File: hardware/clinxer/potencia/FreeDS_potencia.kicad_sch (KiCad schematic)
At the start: 17 parts, among them J1 Screw_Terminal_01x04, J2 Conn_01x04, Q3 BTA26-600BW, U1 MOC3041M, U5 Modulo de Control PWM de pote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

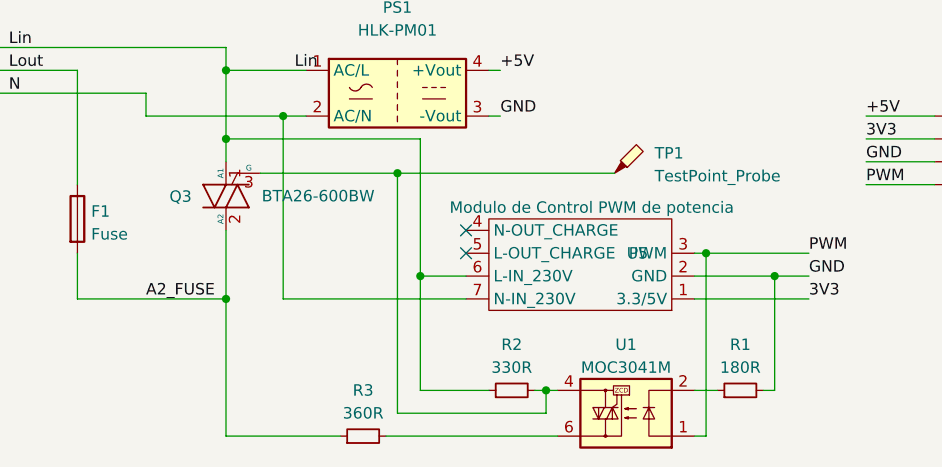
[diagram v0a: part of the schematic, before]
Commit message: Correcciones en arquitectura clinxer
Signed-off-by: Iván Sánchez Ortega <ivan@sanchezortega.es>
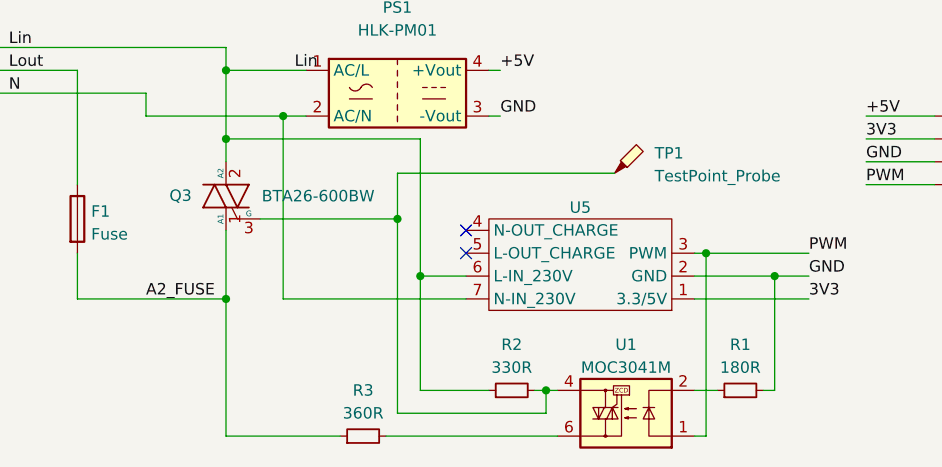
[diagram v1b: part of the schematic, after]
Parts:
- removed U5: Modulo de Control PWM de potencia, Module:YYAC-35 PWM TRIAC, symbol module:YYAC-35_PWM_TRIAC
- added U5: ~, Module:YYAC-3S PWM TRIAC, symbol module:YYAC-3S_PWM_TRIAC
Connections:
- net 3V3: now also U5.1 (3.3/5V)
- net A2_FUSE: now also Q3.1 (A1); no longer Q3.2 (A2)
- net GND: now also U5.2 (GND)
- net Lin: now also Q3.2 (A2), U5.6 (L-IN_230V); no longer Q3.1 (A1)
- net N: now also U5.7 (N-IN_230V)
- net PWM: now also U5.3 (PWM)
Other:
- moved on the sheet: Q3
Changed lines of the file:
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@@
 (kicad_sch (version 20230121) (generator eeschema)
   (paper "A4")
+  (junction (at 109.22 88.9) (diameter 0) (color 0 0 0 0)
+  )
   (junction (at 109.22 81.28) (diameter 0) (color 0 0 0 0)
   )
-  (junction (at 128.27 92.71) (diameter 0) (color 0 0 0 0)
+  (junction (at 128.27 97.79) (diameter 0) (color 0 0 0 0)
   )
   (junction (at 130.81 104.14) (diameter 0) (color 0 0 0 0)
   )
+  (junction (at 109.22 106.68) (diameter 0) (color 0 0 0 0)
+  )
   (junction (at 170.18 104.14) (diameter 0) (color 0 0 0 0)
   )
-  (junction (at 109.22 88.9) (diameter 0) (color 0 0 0 0)
-  )
   (junction (at 162.56 101.6) (diameter 0) (color 0 0 0 0)
-  )
-  (junction (at 109.22 106.68) (diameter 0) (color 0 0 0 0)
   )
   (junction (at 144.78 116.84) (diameter 0) (color 0 0 0 0)
@@
     (stroke (width 0) (type default))
   )
-  (wire (pts (xy 113.03 92.71) (xy 128.27 92.71))
-    (stroke (width 0) (type default))
-  )
   (wire (pts (xy 100.33 86.36) (xy 115.57 86.36))
     (stroke (width 0) (type default))
@@
     (stroke (width 0) (type default))
   )
-  (wire (pts (xy 128.27 92.71) (xy 128.27 119.38))
+  (wire (pts (xy 128.27 92.71) (xy 128.27 97.79))
     (stroke (width 0) (type default))
   )
@@
     (stroke (width 0) (type default))
   )
+  (wire (pts (xy 109.22 99.06) (xy 109.22 106.68))
+    (stroke (width 0) (type default))
+  )
   (wire (pts (xy 161.29 106.68) (xy 173.99 106.68))
     (stroke (width 0) (type default))
@@
     (stroke (width 0) (type default))
   )
+  (wire (pts (xy 113.03 97.79) (xy 128.27 97.79))
+    (stroke (width 0) (type default))
+  )
   (wire (pts (xy 170.18 104.14) (xy 173.99 104.14))
     (stroke (width 0) (type default))
@@
     (stroke (width 0) (type default))
   )
-  (wire (pts (xy 109.22 106.68) (xy 109.22 99.06))
-    (stroke (width 0) (type default))
-  )
   (wire (pts (xy 78.74 78.74) (xy 109.22 78.74))
     (stroke (width 0) (type default))
@@
   )
   (wire (pts (xy 81.28 86.36) (xy 81.28 91.44))
+    (stroke (width 0) (type default))
+  )
+  (wire (pts (xy 128.27 97.79) (xy 128.27 119.38))
     (stroke (width 0) (type default))
   )
@@
     )
   )
-  (symbol (lib_id "Triac_Thyristor:BTA16-600BW") (at 109.22 95.25 180) (unit 1)
+  (symbol (lib_id "Triac_Thyristor:BTA16-600BW") (at 109.22 95.25 0) (mirror y) (unit 1)
     (in_bom yes) (on_board yes) (dnp no)
-    (property "Reference" "Q3" (at 105.41 95.3008 0)
+    (property "Reference" "Q3" (at 105.41 95.1992 0)
       (effects (font (size 1.27 1.27)) (justify left))
     )
@@
       (effects (font (size 1.27 1.27)) (justify left))
     )
-    (property "Footprint" "Package_TO_SOT_THT:TOP3_Vertical" (at 104.14 93.345 0)
+    (property "Footprint" "Package_TO_SOT_THT:TOP3_Vertical" (at 104.14 97.155 0)
       (effects (font (size 1.27 1.27) italic) (justify left) hide)
     )
@@
     )
   )
-  (symbol (lib_id "module:YYAC-35_PWM_TRIAC") (at 153.67 105.41 180) (unit 1)
-    (in_bom yes) (on_board yes) (dnp no)
-    (property "Reference" "U5" (at 154.94 101.6 0)
-      (effects (font (size 1.27 1.27)))
-    )
-    (property "Value" "Modulo de Control PWM de potencia" (at 149.86 96.52 0)
-      (effects (font (size 1.27 1.27)))
-    )
-    (property "Footprint" "Module:YYAC-35 PWM TRIAC" (at 153.67 105.41 0)
+  (symbol (lib_id "Mechanical:MountingHole") (at 21.59 46.99 0) (unit 1)
+    (in_bom yes) (on_board yes) (dnp no) (fields_autoplaced)
+    (property "Reference" "H4" (at 24.13 46.355 0)
+      (effects (font (size 1.27 1.27)) (justify left))
+    )
+    (property "Value" "MountingHole" (at 24.13 48.895 0)
+      (effects (font (size 1.27 1.27)) (justify left))
+    )
+    (property "Footprint" "MountingHole:MountingHole_3.2mm_M3" (at 21.59 46.99 0)
+      (effects (font (size 1.27 1.27)) hide)
+    )
+    (property "Datasheet" "~" (at 21.59 46.99 0)
+      (effects (font (size 1.27 1.27)) hide)
+    )
+    (instances
+      (project "FreeDS_potencia"
+        (path "/82c87a0e-1979-4743-9348-c591e63608f8"
+          (reference "H4") (unit 1)
+        )
+      )
+    )
+  )
+  (symbol (lib_id "Connector:TestPoint_Probe") (at 152.4 92.71 0) (unit 1)
+    (in_bom yes) (on_board yes) (dnp no) (fields_autoplaced)
+    (property "Reference" "TP1" (at 156.845 90.4875 0)
+      (effects (font (size 1.27 1.27)) (justify left))
+    )
+    (property "Value" "TestPoint_Probe" (at 156.845 93.0275 0)
+      (effects (font (size 1.27 1.27)) (justify left))
+    )
+    (property "Footprint" "TestPoint:TestPoint_Loop_D2.50mm_Drill1.0mm" (at 157.48 92.71 0)
+      (effects (font (size 1.27 1.27)) hide)
+    )
+    (property "Datasheet" "~" (at 157.48 92.71 0)
+      (effects (font (size 1.27 1.27)) hide)
+    )
+    (pin "1")
+    (instances
+      (project "FreeDS_potencia"
+        (path "/82c87a0e-1979-4743-9348-c591e63608f8"
+          (reference "TP1") (unit 1)
+        )
+      )
+    )
+  )
+  (symbol (lib_id "Device:Fuse") (at 92.71 97.79 0) (unit 1)
+    (in_bom yes) (on_board yes) (dnp no) (fields_autoplaced)
+    (property "Reference" "F1" (at 94.234 96.9553 0)
+      (effects (font (size 1.27 1.27)) (justify left))
+    )
+    (property "Value" "Fuse" (at 94.234 99.4922 0)
+      (effects (font (size 1.27 1.27)) (justify left))
+    )
+    (property "Footprint" "Fuse:Fuseholder_Clip-5x20mm_Littelfuse_100_Inline_P20.50x4.60mm_D1.30mm_Horizontal" (at 90.932 97.79 90)
+      (effects (font (size 1.27 1.27)) hide)
+    )
+    (property "Datasheet" "~" (at 92.71 97.79 0)
+      (effects (font (size 1.27 1.27)) hide)
+    )
+    (pin "1")
+    (pin "2")
+    (instances
+      (project "FreeDS_potencia"
+        (path "/82c87a0e-1979-4743-9348-c591e63608f8"
+          (reference "F1") (unit 1)
+        )
+      )
+    )
+  )
+  (symbol (lib_id "module:YYAC-3S_PWM_TRIAC") (at 153.67 105.41 180) (unit 1)
+    (in_bom yes) (on_board yes) (dnp no) (fields_autoplaced)
+    (property "Reference" "U5" (at 148.59 96.52 0)
+      (effects (font (size 1.27 1.27)))
+    )
+    (property "Value" "~" (at 153.67 105.41 0)
+      (effects (font (size 1.27 1.27)))
+    )
+    (property "Footprint" "Module:YYAC-3S PWM TRIAC" (at 153.67 105.41 0)
       (effects (font (size 1.27 1.27)) hide)
     )
@@
         )
       )
-    )
-  )
-  (symbol (lib_id "Mechanical:MountingHole") (at 21.59 46.99 0) (unit 1)
-    (in_bom yes) (on_board yes) (dnp no) (fields_autoplaced)
-    (property "Reference" "H4" (at 24.13 46.355 0)
-      (effects (font (size 1.27 1.27)) (justify left))
-    )
-    (property "Value" "MountingHole" (at 24.13 48.895 0)
-      (effects (font (size 1.27 1.27)) (justify left))
-    )
-    (property "Footprint" "MountingHole:MountingHole_3.2mm_M3" (at 21.59 46.99 0)
-      (effects (font (size 1.27 1.27)) hide)
-    )
-    (property "Datasheet" "~" (at 21.59 46.99 0)
-      (effects (font (size 1.27 1.27)) hide)
-    )
-    (instances
-      (project "FreeDS_potencia"
-        (path "/82c87a0e-1979-4743-9348-c591e63608f8"
-          (reference "H4") (unit 1)
-        )
-      )
-    )
-  )
-  (symbol (lib_id "Connector:TestPoint_Probe") (at 152.4 92.71 0) (unit 1)
-    (in_bom yes) (on_board yes) (dnp no) (fields_autoplaced)
-    (property "Reference" "TP1" (at 156.845 90.4875 0)
-      (effects (font (size 1.27 1.27)) (justify left))
-    )
-    (property "Value" "TestPoint_Probe" (at 156.845 93.0275 0)
-      (effects (font (size 1.27 1.27)) (justify left))
-    )
-    (property "Footprint" "TestPoint:TestPoint_Loop_D2.50mm_Drill1.0mm" (at 157.48 92.71 0)
-      (effects (font (size 1.27 1.27)) hide)
-    )
-    (property "Datasheet" "~" (at 157.48 92.71 0)
-      (effects (font (size 1.27 1.27)) hide)
-    )
-    (pin "1")
-    (instances
-      (project "FreeDS_potencia"
-        (path "/82c87a0e-1979-4743-9348-c591e63608f8"
-          (reference "TP1") (unit 1)
-        )
-      )
-    )
-  )
-  (symbol (lib_id "Device:Fuse") (at 92.71 97.79 0) (unit 1)
-    (in_bom yes) (on_board yes) (dnp no) (fields_autoplaced)
-    (property "Reference" "F1" (at 94.234 96.9553 0)
-      (effects (font (size 1.27 1.27)) (justify left))
-    )
-    (property "Value" "Fuse" (at 94.234 99.4922 0)
-      (effects (font (size 1.27 1.27)) (justify left))
-    )
-    (property "Footprint" "Fuse:Fuseholder_Clip-5x20mm_Littelfuse_100_Inline_P20.50x4.60mm_D1.30mm_Horizontal" (at 90.932 97.79 90)
-      (effects (font (size 1.27 1.27)) hide)
-    )
-    (property "Datasheet" "~" (at 92.71 97.79 0)
-      (effects (font (size 1.27 1.27)) hide)
-    )
-    (pin "1")
-    (pin "2")
-    (instances
-      (project "FreeDS_potencia"
-        (path "/82c87a0e-1979-4743-9348-c591e63608f8"
-          (reference "F1") (unit 1)
-        )
-      )

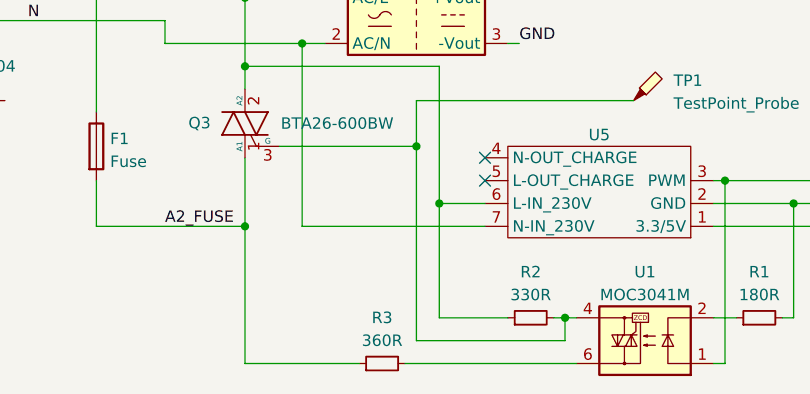
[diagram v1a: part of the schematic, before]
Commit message: Corrección arq. clinxer: pines de optoacoplador
Signed-off-by: Iván Sánchez Ortega <ivan@sanchezortega.es>
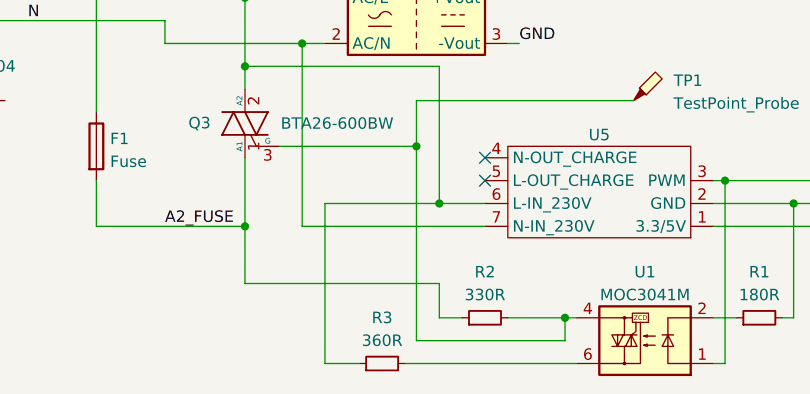
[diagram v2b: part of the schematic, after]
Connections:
- net A2_FUSE: now also R2.1; no longer R3.1
- net Lin: now also R3.1; no longer R2.1
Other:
- moved on the sheet: R2
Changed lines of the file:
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@@
     (stroke (width 0) (type default))
   )
-  (wire (pts (xy 138.43 116.84) (xy 130.81 116.84))
+  (wire (pts (xy 133.35 116.84) (xy 130.81 116.84))
     (stroke (width 0) (type default))
   )
@@
     (stroke (width 0) (type default))
   )
-  (wire (pts (xy 130.81 116.84) (xy 130.81 104.14))
-    (stroke (width 0) (type default))
-  )
   (wire (pts (xy 180.34 88.9) (xy 187.96 88.9))
     (stroke (width 0) (type default))
   )
-  (wire (pts (xy 143.51 116.84) (xy 144.78 116.84))
+  (wire (pts (xy 118.11 104.14) (xy 118.11 121.92))
+    (stroke (width 0) (type default))
+  )
+  (wire (pts (xy 138.43 116.84) (xy 144.78 116.84))
     (stroke (width 0) (type default))
   )
@@
     (stroke (width 0) (type default))
   )
+  (wire (pts (xy 130.81 116.84) (xy 130.81 113.03))
+    (stroke (width 0) (type default))
+  )
   (wire (pts (xy 128.27 92.71) (xy 152.4 92.71))
     (stroke (width 0) (type default))
@@
     (stroke (width 0) (type default))
   )
+  (wire (pts (xy 109.22 113.03) (xy 109.22 106.68))
+    (stroke (width 0) (type default))
+  )
   (wire (pts (xy 109.22 81.28) (xy 109.22 78.74))
     (stroke (width 0) (type default))
@@
     (stroke (width 0) (type default))
   )
+  (wire (pts (xy 130.81 113.03) (xy 109.22 113.03))
+    (stroke (width 0) (type default))
+  )
   (wire (pts (xy 115.57 106.68) (xy 115.57 86.36))
     (stroke (width 0) (type default))
   )
-  (wire (pts (xy 121.92 121.92) (xy 109.22 121.92))
+  (wire (pts (xy 121.92 121.92) (xy 118.11 121.92))
     (stroke (width 0) (type default))
   )
@@
     (stroke (width 0) (type default))
   )
-  (wire (pts (xy 109.22 121.92) (xy 109.22 106.68))
-    (stroke (width 0) (type default))
-  )
   (wire (pts (xy 180.34 86.36) (xy 187.96 86.36))
     (stroke (width 0) (type default))
@@
     (stroke (width 0) (type default))
   )
+  (wire (pts (xy 130.81 104.14) (xy 135.89 104.14))
+    (stroke (width 0) (type default))
+  )
   (wire (pts (xy 130.81 88.9) (xy 130.81 104.14))
     (stroke (width 0) (type default))
@@
     (stroke (width 0) (type default))
   )
-  (wire (pts (xy 130.81 104.14) (xy 135.89 104.14))
+  (wire (pts (xy 118.11 104.14) (xy 130.81 104.14))
     (stroke (width 0) (type default))
   )
@@
     )
   )
-  (symbol (lib_id "Device:R_Small") (at 140.97 116.84 90) (unit 1)
-    (in_bom yes) (on_board yes) (dnp no) (fields_autoplaced)
-    (property "Reference" "R2" (at 140.97 111.76 90)
-      (effects (font (size 1.27 1.27)))
-    )
-    (property "Value" "330R" (at 140.97 114.3 90)
-      (effects (font (size 1.27 1.27)))
-    )
-    (property "Footprint" "Resistor_THT:R_Axial_DIN0207_L6.3mm_D2.5mm_P10.16mm_Horizontal" (at 140.97 116.84 0)
-      (effects (font (size 1.27 1.27)) hide)
-    )
-    (property "Datasheet" "~" (at 140.97 116.84 0)
-      (effects (font (size 1.27 1.27)) hide)
-    )
+  (symbol (lib_id "Device:R_Small") (at 135.89 116.84 90) (unit 1)
+    (in_bom yes) (on_board yes) (dnp no) (fields_autoplaced)
+    (property "Reference" "R2" (at 135.89 111.76 90)
+      (effects (font (size 1.27 1.27)))
+    )
+    (property "Value" "330R" (at 135.89 114.3 90)
+      (effects (font (size 1.27 1.27)))
+    )
+    (property "Footprint" "Resistor_THT:R_Axial_DIN0207_L6.3mm_D2.5mm_P10.16mm_Horizontal" (at 135.89 116.84 0)
+      (effects (font (size 1.27 1.27)) hide)
+    )
+    (property "Datasheet" "~" (at 135.89 116.84 0)
+      (effects (font (size 1.27 1.27)) hide)
+    )
